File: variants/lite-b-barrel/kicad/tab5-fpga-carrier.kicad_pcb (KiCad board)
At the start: 4 copper layers, 99 x 78 mm, 105 parts, among them J1 DC 12V ONLY, J3 M5-BUS (to Tab5), J4 SOCKET XDAP-4042044-20401, J5 HDMI OUT, J6 PMOD1, J7 PMOD2, J8 GPIO pads, Q1 2N7002, Q2 2N7002, Q3 2N7002, Q4 2N7002, SW1 SW, SW2 RESET (Tab5), SW3 FPGA ON/OFF, U10 TPS3839K50DBZR, U2 TPS5430DDAR, U3 XC6206P332MR-G, U4 RCLAMP0524P, U5 RCLAMP0524P, U6 SRV05-4, U7 SN74CB3Q3245PWR, U8 SN74CB3Q3245PWR, U9 TPS3839G33DBZR

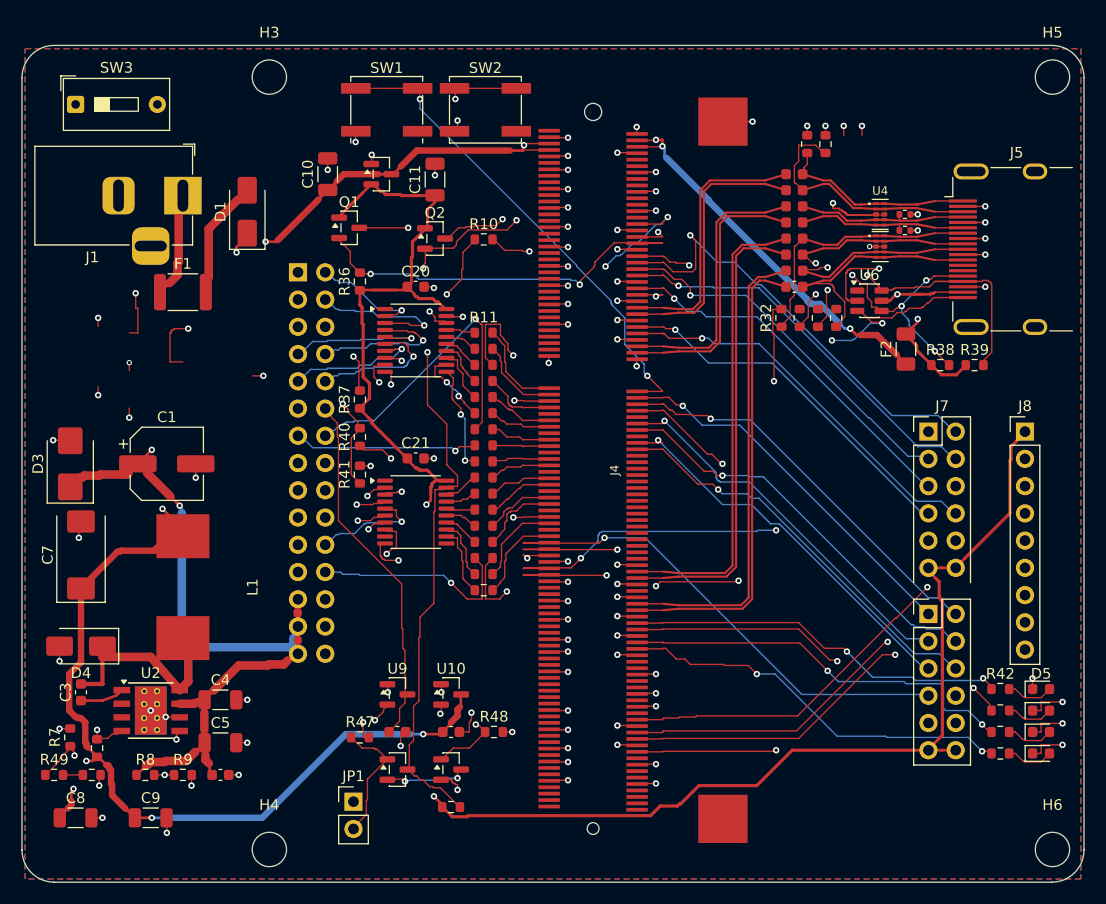
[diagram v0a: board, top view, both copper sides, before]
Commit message: Qualify lite variants for conditional PoC fabrication and publish per-board reports
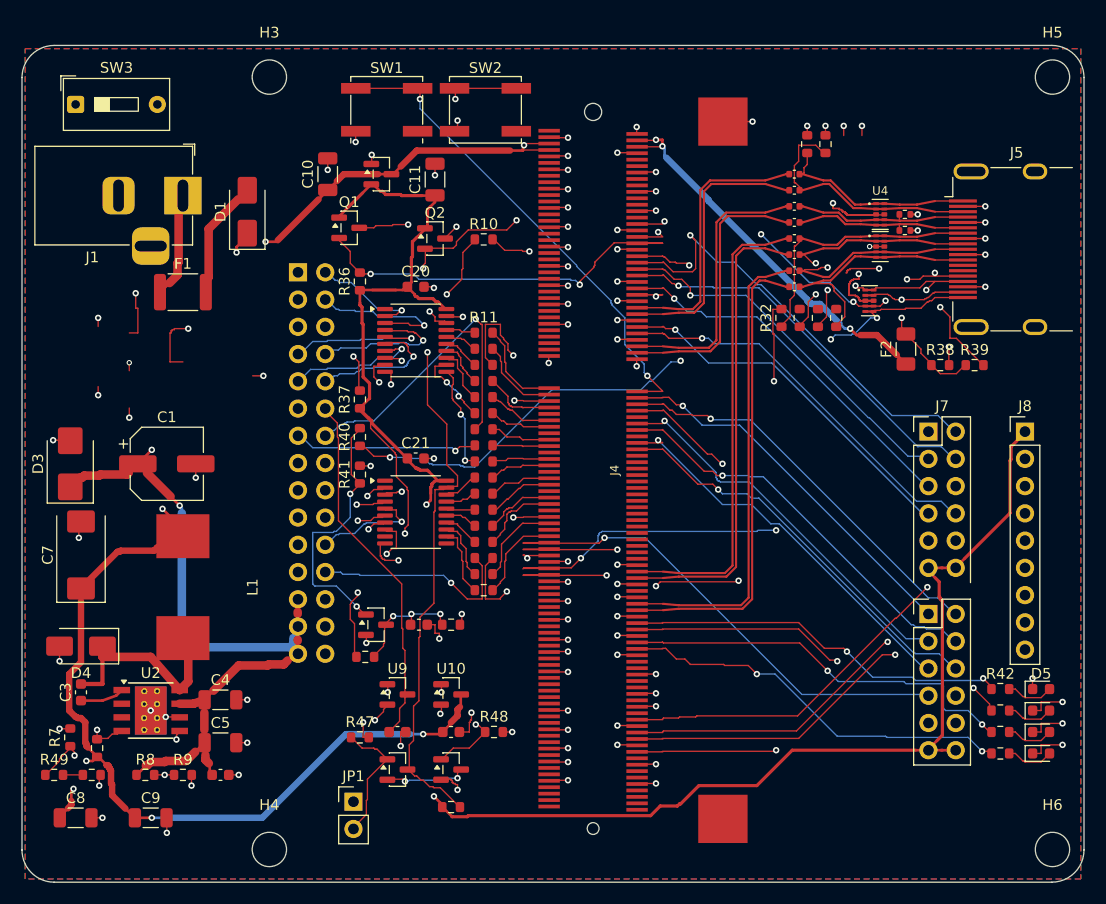
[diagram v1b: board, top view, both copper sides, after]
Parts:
- added C24: 100n, C_0603_1608Metric, F.Cu at (65.0, 55.0)
- added Q5: MMBT3904, SOT-23, F.Cu at (61.0, 55.0)
- added R51: 47k, R_0603_1608Metric, F.Cu at (60.0, 58.0)
- added R52: 10k, R_0603_1608Metric, F.Cu at (68.0, 55.0)
- C12, C13, C14, C15, C16, C17, C18, C19: footprint C_0603_1608Metric -> C_0402_1005Metric
- R10, R11, R12, R13, R14, R15, R16, R19, R20, R21, R22, R23, R24, R26, R27: value 33R -> 680R
- R40: value 10k -> 47k
- R41: value 20k -> 100k
- U6: value SRV05-4 -> RCLAMP0524P; footprint SOT-23-6 -> DFN2510-10L_RCLAMP0524P
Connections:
- R40 pad 2: F_HPD -> HPD_B
- R41 pad 1: F_HPD -> HPD_B
- U6 pad 1: (no net) -> HDMI_SDA
- U6 pad 2: GND -> HDMI_5V
- U6 pad 3: HDMI_HPD -> GND
- U6 pad 5: HDMI_5V -> HDMI_HPD
- U6 pad 6: HDMI_SDA -> HDMI_HPD
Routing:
- net +3V3: track 170.7 -> 198.2 mm, vias 2 -> 4
- net HPD_B: track 0.00 -> 24.4 mm, vias 0 -> 2
- net HPD_BUF: track 0.00 -> 11.2 mm, vias 0 -> 3
- net GND: track 197.6 -> 208.4 mm, vias 107 -> 110
- net HDMI_SCL: track 69.3 -> 72.8 mm, vias 5 -> 7
- net HDMI_SDA: track 66.0 -> 64.1 mm, vias 2 -> 4
- net F_HPD: track 49.4 -> 48.2 mm, vias 3 -> 2
- net HDMI_HPD: track 66.9 -> 66.0 mm, vias 3 -> 4
- net HDMI_5V: track 20.9 -> 21.5 mm

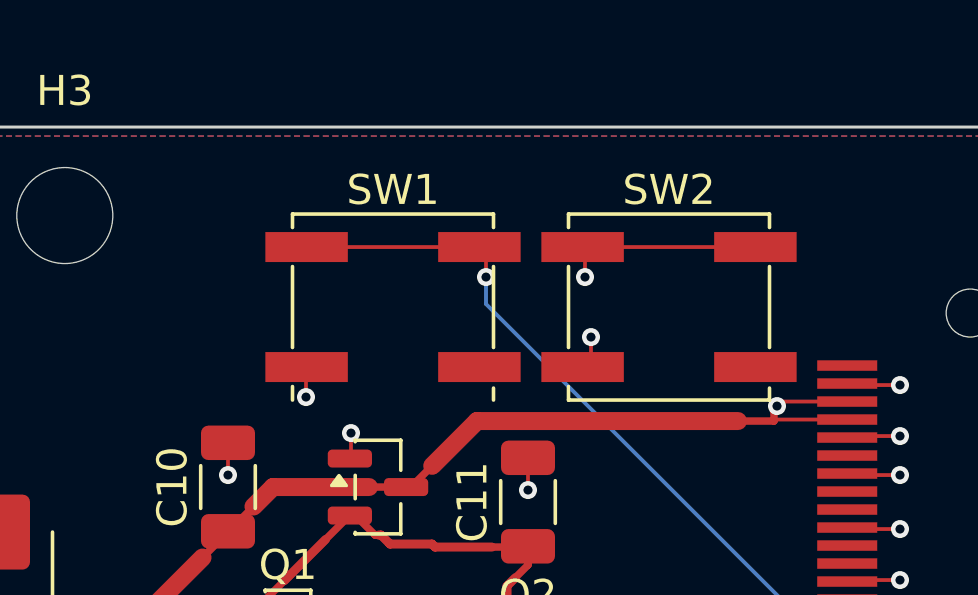
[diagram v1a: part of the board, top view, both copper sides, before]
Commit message: Align variants B and C with Akizuki buttons and explain A BOM
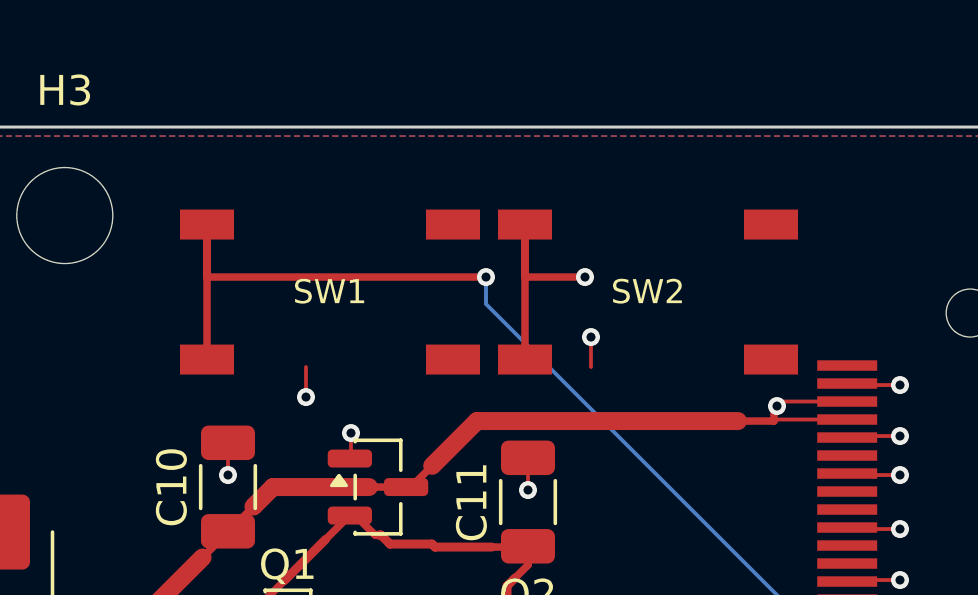
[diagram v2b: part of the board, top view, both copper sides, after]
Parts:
- SW1: value SW -> TS-06104; footprint SW_SPST_EVQP0 -> carrier:SW_TS_06104_HandSolder
- SW2: value RESET (Tab5) -> TS-06104; footprint SW_SPST_EVQP0 -> carrier:SW_TS_06104_HandSolder
- moved SW1 2.16 mm to (59.9, 6.50)
- moved SW2 0.86 mm to (70.5, 6.50)
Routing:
- net F_BTN0: track 45.8 -> 54.5 mm
- net TAB_RST: track 33.1 -> 34.5 mm
